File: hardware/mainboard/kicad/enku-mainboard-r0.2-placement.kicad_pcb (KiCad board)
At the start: 4 copper layers, 59 x 101 mm, 122 parts, among them J1 1S LiPo + NTC, J2 Hirose DM3AT-SF-PEJM5, J3 FH34SRJ-24S-0.5SH(50), J5 GCT USB4105-GF-A-120, J6 4-pin pogo dock, J7 Tag-Connect TC2030-IDC-NL, Q1 IRLML6346TRPBF, SW1 HARD POWER, SW2 BOOT / RECOVERY, SW3 BTN_L1, SW4 BTN_L2, SW5 BTN_R1, SW6 BTN_R2, U1 ESP32-S3-WROOM-1-N16R8, U2 TPS2121, U3 BQ25185DLHR, U4 TPS63802DLAR, U5 BMI270, U6 DRV5032FBDBZR, U8 USBLC6-2SC6

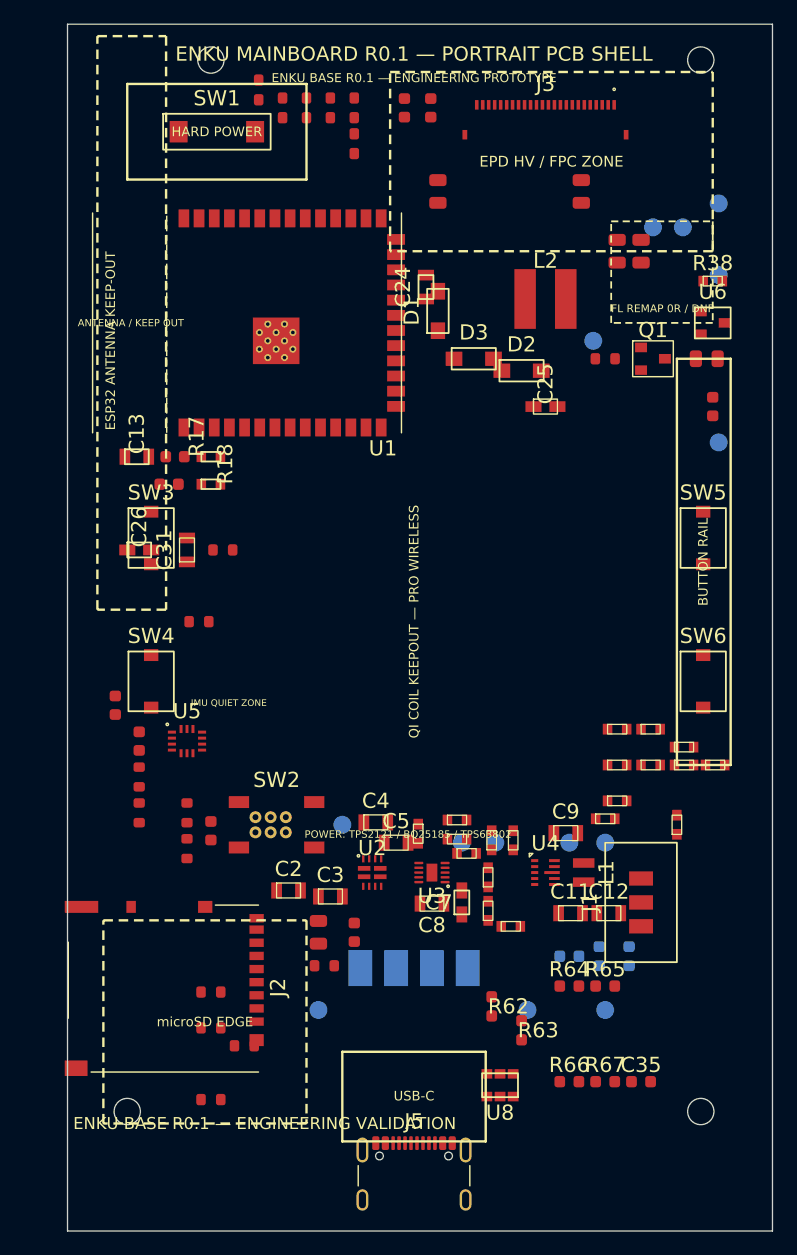
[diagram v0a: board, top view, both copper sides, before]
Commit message: mechanical: reposition four rear M2 mounts; retain USB NPTH/PTH; gate holes and display stack
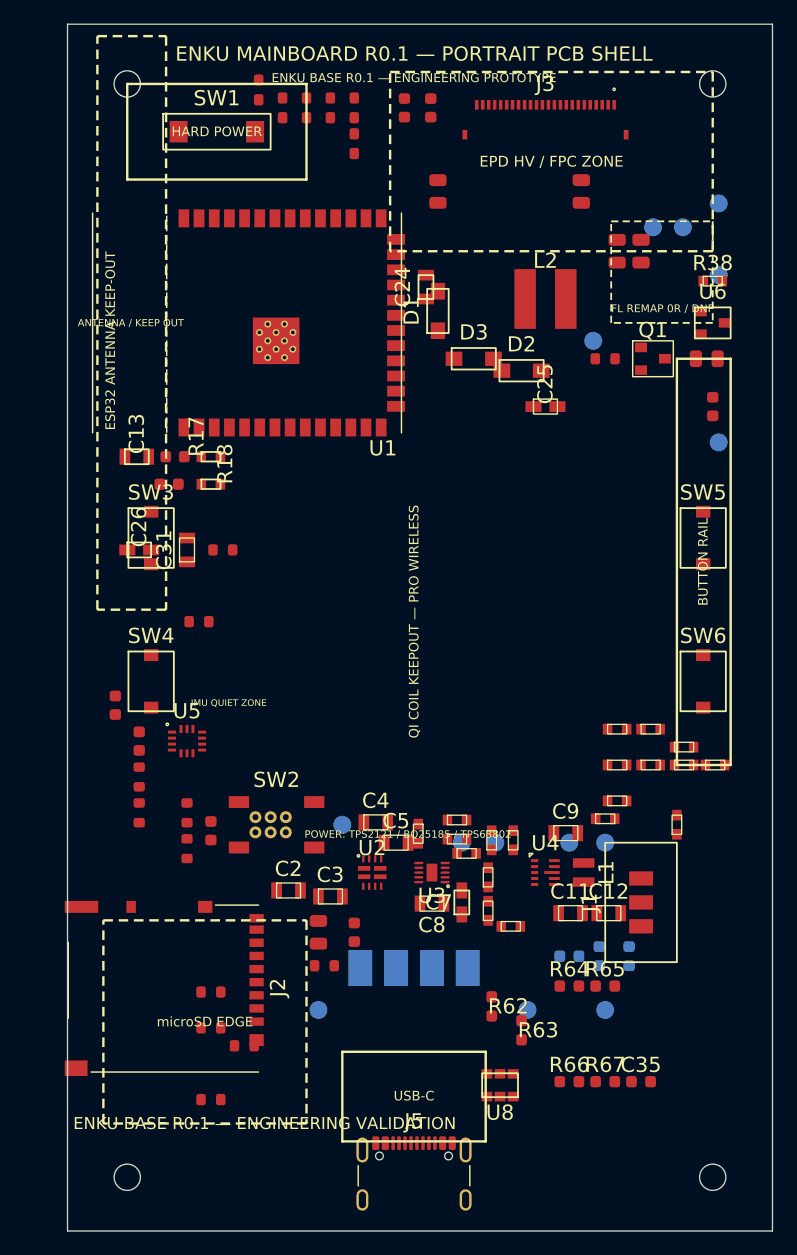
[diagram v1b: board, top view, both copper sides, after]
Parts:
- moved H1 7.28 mm to (23.0, 25.0)
- moved H4 5.59 mm to (72.0, 116.5)
- moved H3 5.50 mm to (23.0, 116.5)
- moved H2 2.24 mm to (72.0, 25.0)
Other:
- board text added: "H1 REAR M2 - BOSS DIA >=5.5 EVAL"
- board text added: "H2 REAR M2 - BOSS DIA >=5.5 EVAL"
- board text added: "H3 REAR M2 - BOSS DIA >=5.5 EVAL"
- board text added: "H4 REAR M2 - BOSS DIA >=5.5 EVAL"
- board text added: "NOMINAL CENTERED GDEY0397T81P MODULE PROJECTION - NOT FPC DATUM"
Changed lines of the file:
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@@
     (at 46 117.7) (layer "Dwgs.User")
     (effects (font (size 0.65 0.65) (thickness 0.12))))
+  (gr_rect (start 19.38 22.19) (end 75.62 118.81)
+    (stroke (width 0.12) (type dash)) (fill none) (layer "Dwgs.User"))
+  (gr_text "NOMINAL CENTERED GDEY0397T81P MODULE PROJECTION - NOT FPC DATUM"
+    (at 47.5 21) (layer "Dwgs.User")
+    (effects (font (size 0.55 0.55) (thickness 0.10))))
+  (gr_circle (center 23 25) (end 25.75 25)
+    (stroke (width 0.10) (type dash)) (fill none) (layer "Dwgs.User"))
+  (gr_text "H1 REAR M2 - BOSS DIA >=5.5 EVAL"
+    (at 23 29.20) (layer "Dwgs.User")
+    (effects (font (size 0.55 0.55) (thickness 0.10))))
+  (gr_circle (center 72 25) (end 74.75 25)
+    (stroke (width 0.10) (type dash)) (fill none) (layer "Dwgs.User"))
+  (gr_text "H2 REAR M2 - BOSS DIA >=5.5 EVAL"
+    (at 72 29.20) (layer "Dwgs.User")
+    (effects (font (size 0.55 0.55) (thickness 0.10))))
+  (gr_circle (center 23 116.5) (end 25.75 116.5)
+    (stroke (width 0.10) (type dash)) (fill none) (layer "Dwgs.User"))
+  (gr_text "H3 REAR M2 - BOSS DIA >=5.5 EVAL"
+    (at 23 112.30) (layer "Dwgs.User")
+    (effects (font (size 0.55 0.55) (thickness 0.10))))
+  (gr_circle (center 72 116.5) (end 74.75 116.5)
+    (stroke (width 0.10) (type dash)) (fill none) (layer "Dwgs.User"))
+  (gr_text "H4 REAR M2 - BOSS DIA >=5.5 EVAL"
+    (at 72 112.30) (layer "Dwgs.User")
+    (effects (font (size 0.55 0.55) (thickness 0.10))))
   (gr_rect (start 18 20) (end 77 121)
     (stroke (width 0.05) (type default)) (fill none) (layer "Edge.Cuts"))
@@
     (effects (font (size 1 1) (thickness 0.15))))
   (footprint "MountingHole:MountingHole_2.2mm_M2" (layer "F.Cu")
-    (at 30 23)
+    (at 23 25)
     (attr board_only exclude_from_pos_files exclude_from_bom)
     (property "Reference" "H1" (at 0 -3 0) (layer "F.SilkS") hide)
@@
     (pad "" np_thru_hole circle (at 0 0) (size 2.2 2.2) (drill 2.2) (layers "*.Cu" "*.Mask")))
   (footprint "MountingHole:MountingHole_2.2mm_M2" (layer "F.Cu")
-    (at 71 23)
+    (at 72 25)
     (attr board_only exclude_from_pos_files exclude_from_bom)
     (property "Reference" "H2" (at 0 -3 0) (layer "F.SilkS") hide)
@@
     (pad "" np_thru_hole circle (at 0 0) (size 2.2 2.2) (drill 2.2) (layers "*.Cu" "*.Mask")))
   (footprint "MountingHole:MountingHole_2.2mm_M2" (layer "F.Cu")
-    (at 23 111)
+    (at 23 116.5)
     (attr board_only exclude_from_pos_files exclude_from_bom)
     (property "Reference" "H3" (at 0 3 0) (layer "F.SilkS") hide)
@@
     (pad "" np_thru_hole circle (at 0 0) (size 2.2 2.2) (drill 2.2) (layers "*.Cu" "*.Mask")))
   (footprint "MountingHole:MountingHole_2.2mm_M2" (layer "F.Cu")
-    (at 71 111)
+    (at 72 116.5)
     (attr board_only exclude_from_pos_files exclude_from_bom)
     (property "Reference" "H4" (at 0 3 0) (layer "F.SilkS") hide)

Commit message: mechanical: block J3 FPC assembly until exact GDEY0397T81P tail drawing and pin1 verification
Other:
- board text added: "J3 FPC ROUTE NOT VERIFIED - FREE END/CONTACT SIDE UNKNOWN"
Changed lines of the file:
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@@
     (at 72 69 90) (layer "Dwgs.User")
     (effects (font (size 0.55 0.55) (thickness 0.10))))
+  (gr_text "J3 FPC ROUTE NOT VERIFIED - FREE END/CONTACT SIDE UNKNOWN"
+    (at 58.0 34.0) (layer "Dwgs.User")
+    (effects (font (size 0.50 0.50) (thickness 0.09))))
   (gr_text "R25 PLACEMENT STUDY - NO ROUTING / NO PRODUCTION"
     (at 46 117.7) (layer "Dwgs.User")

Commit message: mechanical: mark exact Good Display stepped FPC tail and J3/H2 placement collision
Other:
- board text added: "J3 CANDIDATE x69.37 y34 - NO PADS / NO ROUTE"
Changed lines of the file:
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@@
     (at 72 69 90) (layer "Dwgs.User")
+    (effects (font (size 0.55 0.55) (thickness 0.10))))
+  (gr_rect (start 62.12 31.75) (end 76.62 36.05)
+    (stroke (width 0.15) (type dash)) (fill none) (layer "Dwgs.User"))
+  (gr_text "J3 CANDIDATE x69.37 y34 - NO PADS / NO ROUTE"
+    (at 47.5 40) (layer "Dwgs.User")
     (effects (font (size 0.55 0.55) (thickness 0.10))))
   (gr_text "J3 FPC ROUTE NOT VERIFIED - FREE END/CONTACT SIDE UNKNOWN"
